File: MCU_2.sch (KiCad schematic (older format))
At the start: 18 parts, among them U2 STM32F051K6Ux

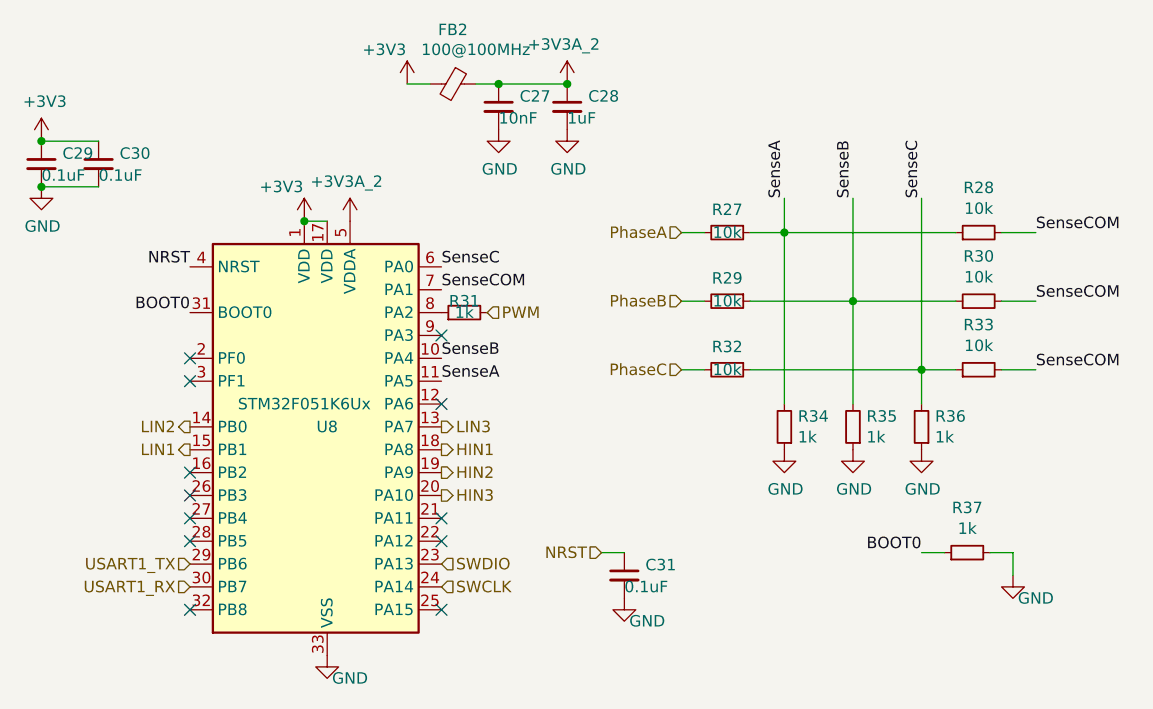
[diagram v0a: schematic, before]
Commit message: Lots of changes made with back being rerouted
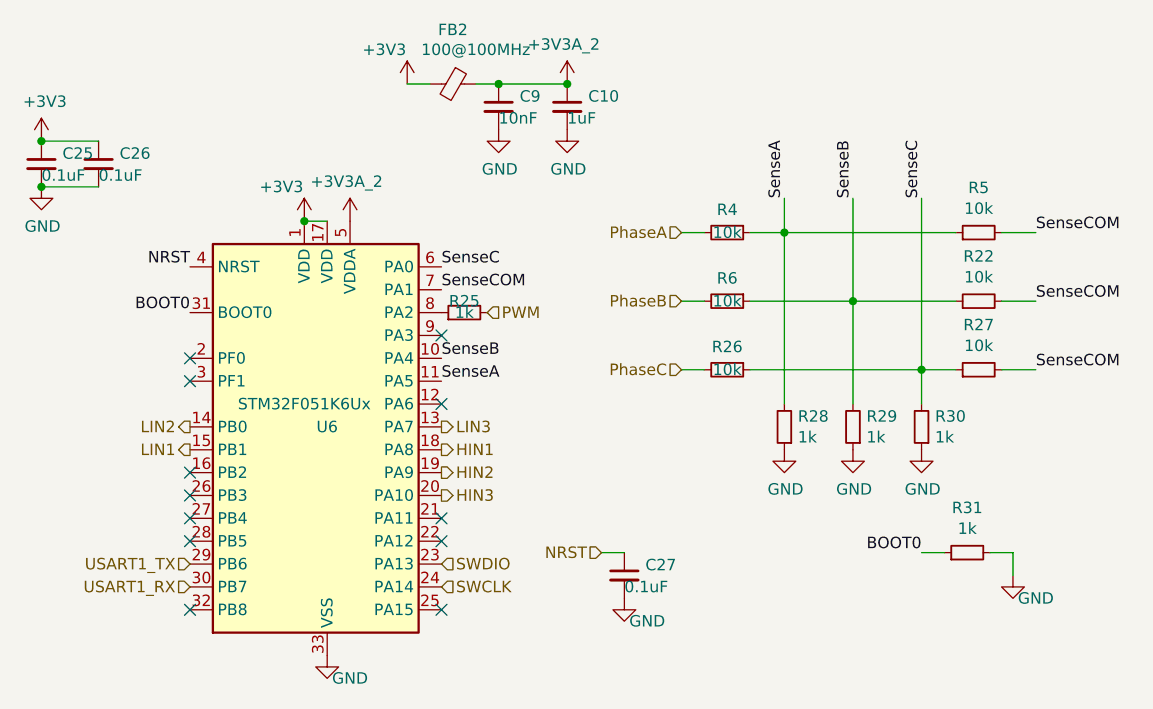
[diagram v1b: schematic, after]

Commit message: Added stuff
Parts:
- removed R24: 1k, Resistor_SMD:R_0402_1005Metric, symbol Device:R_Small
- removed U2: STM32F051K6Ux, Package_DFN_QFN:QFN-32-1EP_5x5mm_P0.5mm_EP3.45x3.45mm, symbol MCU_ST_STM32F0:STM32F051K6Ux
- added R25: 1k, Resistor_SMD:R_0402_1005Metric, symbol Device:R_Small
- added U6: STM32F051K6Ux, Package_DFN_QFN:QFN-32-1EP_5x5mm_P0.5mm_EP3.45x3.45mm, symbol MCU_ST_STM32F0:STM32F051K6Ux
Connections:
- net +3.3VA_2: now also U6.5 (VDDA)
- net +3V3: now also U6.1 (VDD), U6.17 (VDD)
- net BOOT0: now also U6.31 (BOOT0)
- net GND: now also U6.33 (VSS)
- net HIN1: now also U6.18 (PA8)
- net HIN2: now also U6.19 (PA9)
- net HIN3: now also U6.20 (PA10)
- net LIN1: now also U6.15 (PB1)
- net LIN2: now also U6.14 (PB0)
- net LIN3: now also U6.13 (PA7)
- net NRST: now also U6.4 (NRST)
- net PWM: now also R25.2
- net SWCLK: now also U6.24 (PA14)
- net SWDIO: now also U6.23 (PA13)
- net SenseA: now also U6.11 (PA5)
- net SenseB: now also U6.10 (PA4)
- net SenseC: now also U6.6 (PA0)
- net SenseCOM: now also U6.7 (PA1)
- net USART1_RX: now also U6.30 (PB7)
- net USART1_TX: now also U6.29 (PB6)
- new net: R25.1, U6.8 (PA2)
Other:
- moved on the sheet: C27
